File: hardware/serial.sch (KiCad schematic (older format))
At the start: 19 parts

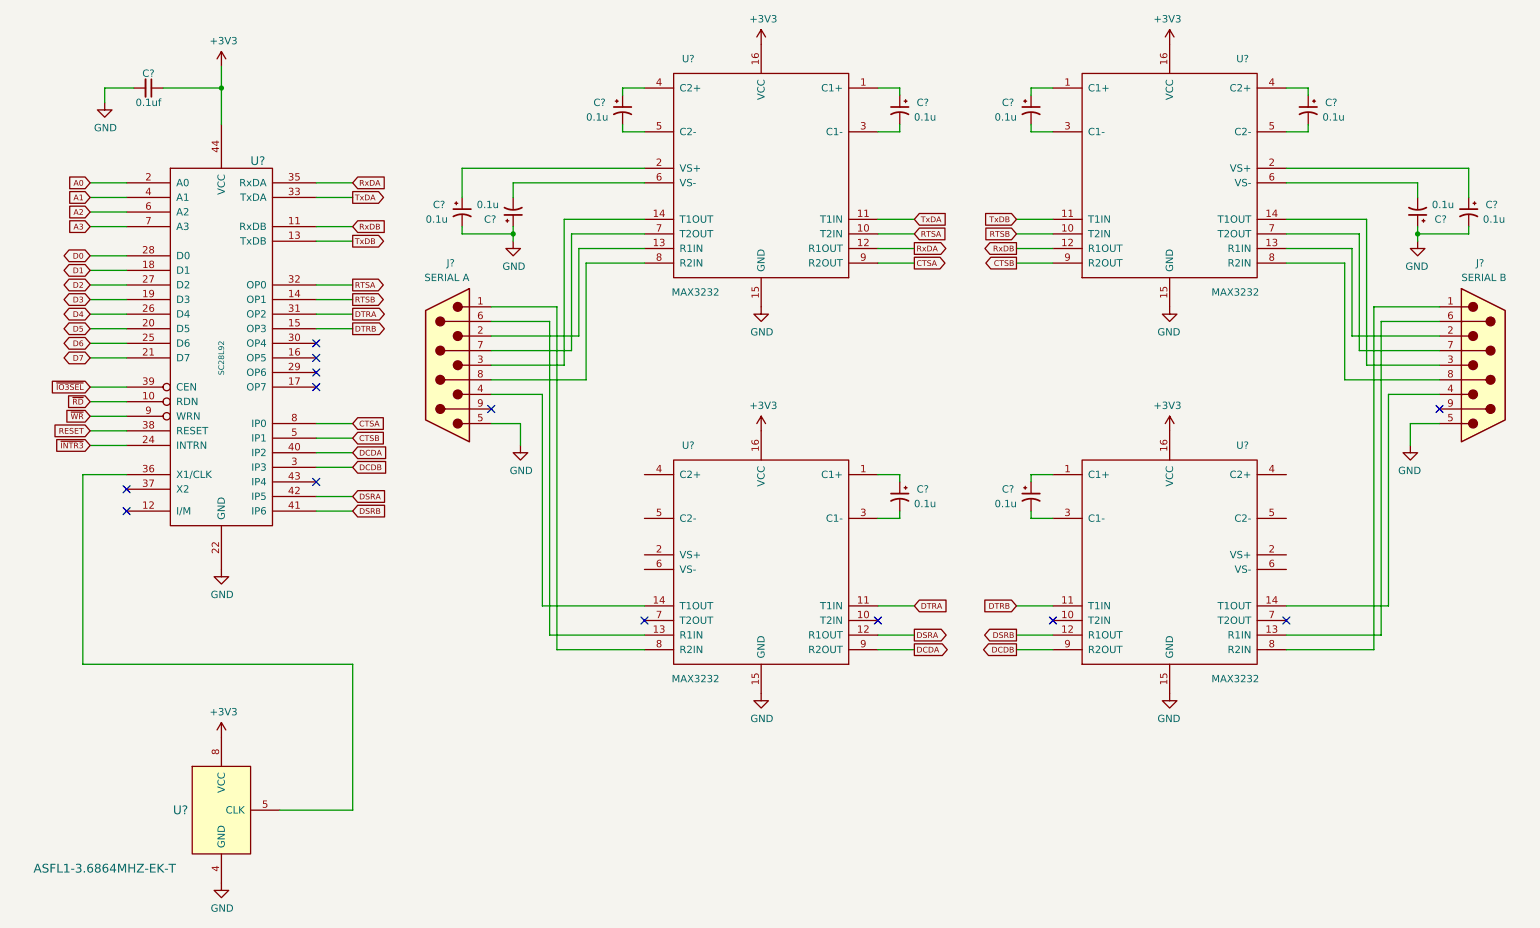
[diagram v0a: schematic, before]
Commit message: Add SPI and missing caps on MAX3232s.
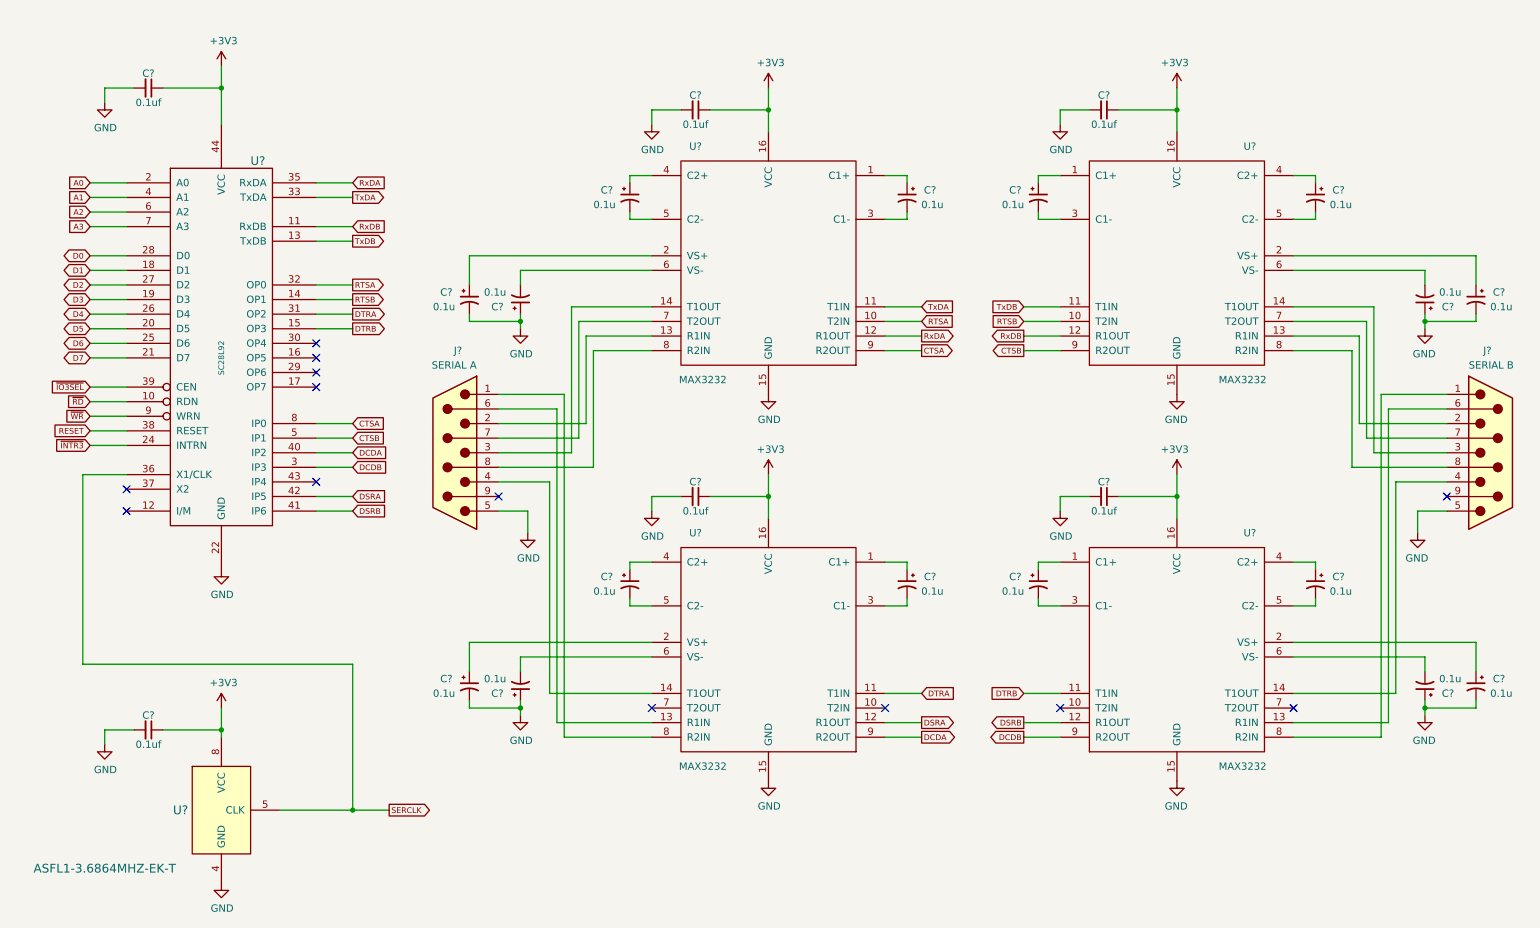
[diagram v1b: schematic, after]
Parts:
- added C? (x5): 0.1uf, symbol Device:C_Small
- added C? (x6): 0.1u, symbol Device:CP1_Small
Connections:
- net +3V3: now also C?.1, C?.1, C?.1, C?.1, C?.1
- net GND: now also C?.1, C?.1, C?.2, C?.2, C?.2, C?.2, C?.2, C?.2, C?.2
- net at U?.2 (VS+): now also C?.1 (x2)
- net at U?.4 (C2+): now also C?.1 (x2)
- net at U?.5 (C2-): now also C?.2 (x2)
- net at U?.6 (VS-): now also C?.2 (x2)
- net SERCLK: now reaches U?.36 (X1/CLK), U?.5 (CLK)
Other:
- moved on the sheet: C?, J?, U?

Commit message: Combine VIA, SPI, and UART into a single io.sch sheet. The serial.sch sheet is now just the serial ports and the line drivers.
Add ports.sch sheet for remaining I/O ports.
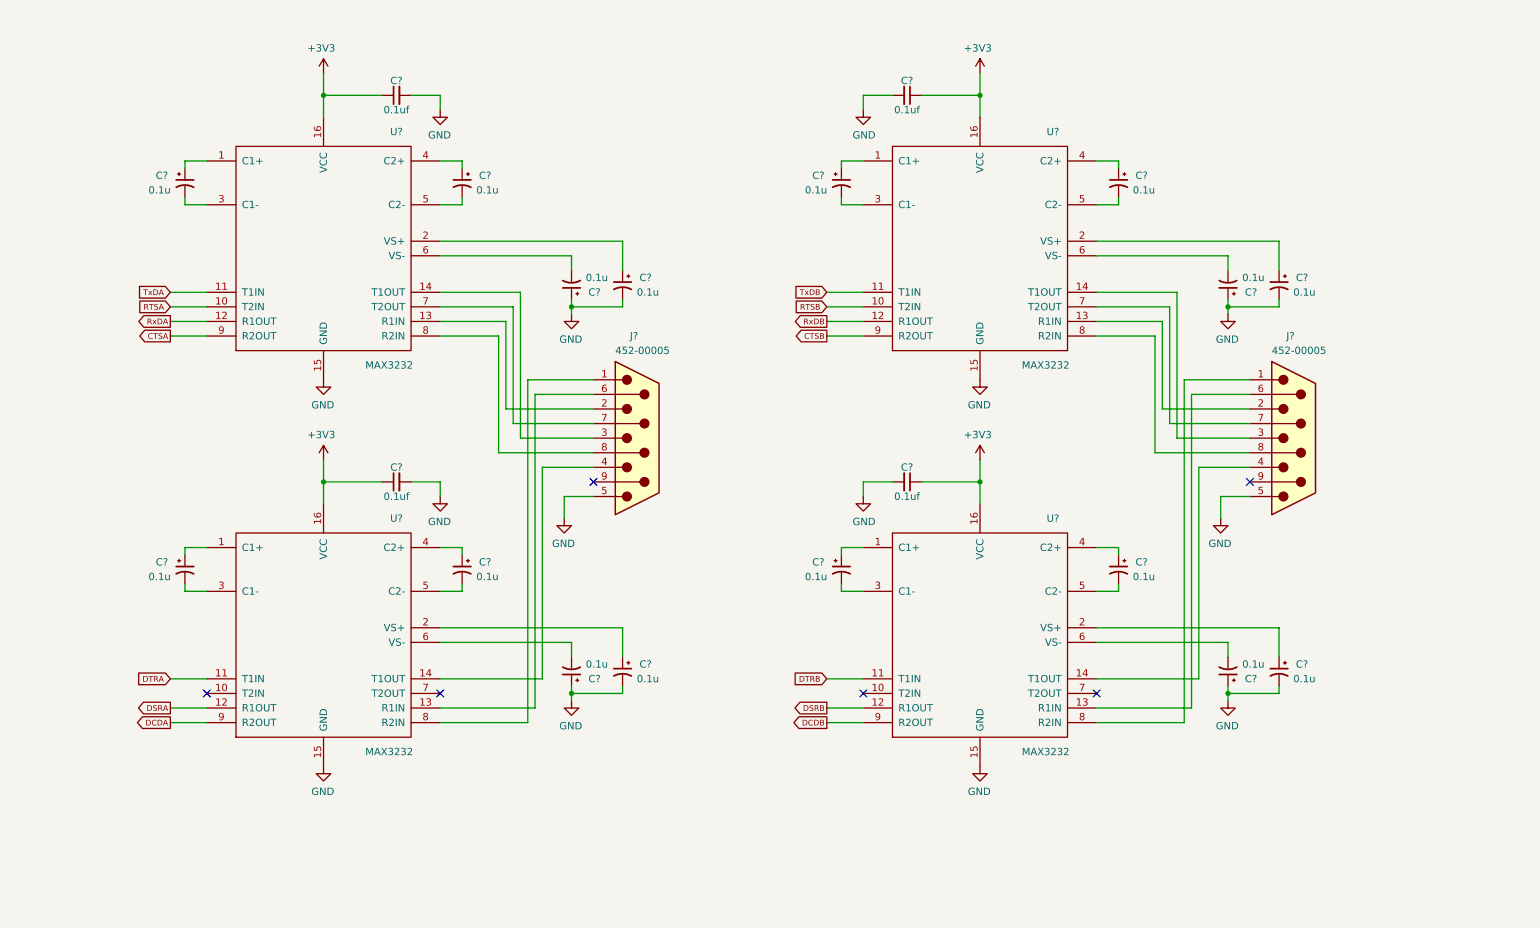
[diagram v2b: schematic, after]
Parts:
- removed C? (x2): 0.1uf, symbol Device:C_Small
- removed U?: SC28L92, Package_LCC:PLCC-44_THT-Socket, symbol SC28L92:SC28L92
- removed U?: ASFL1-3.6864MHZ-EK-T, symbol osc:Osc_8pin
- J?: value SERIAL A -> 452-00005
- J?: value SERIAL B -> 452-00005
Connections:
- no-connect marks 13 -> 6
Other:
- moved on the sheet: C?, J?, U?
